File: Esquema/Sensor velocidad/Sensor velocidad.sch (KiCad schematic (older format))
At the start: 49 parts, among them J1 DB9_Female_MountingHoles, J2 DB9_Male_MountingHoles, J3 DB9_Female_MountingHoles, J4 DB9_Male_MountingHoles, J5 Conn_01x02_Male, U1 TCRT5000_GD, U2 TCRT5000_GD

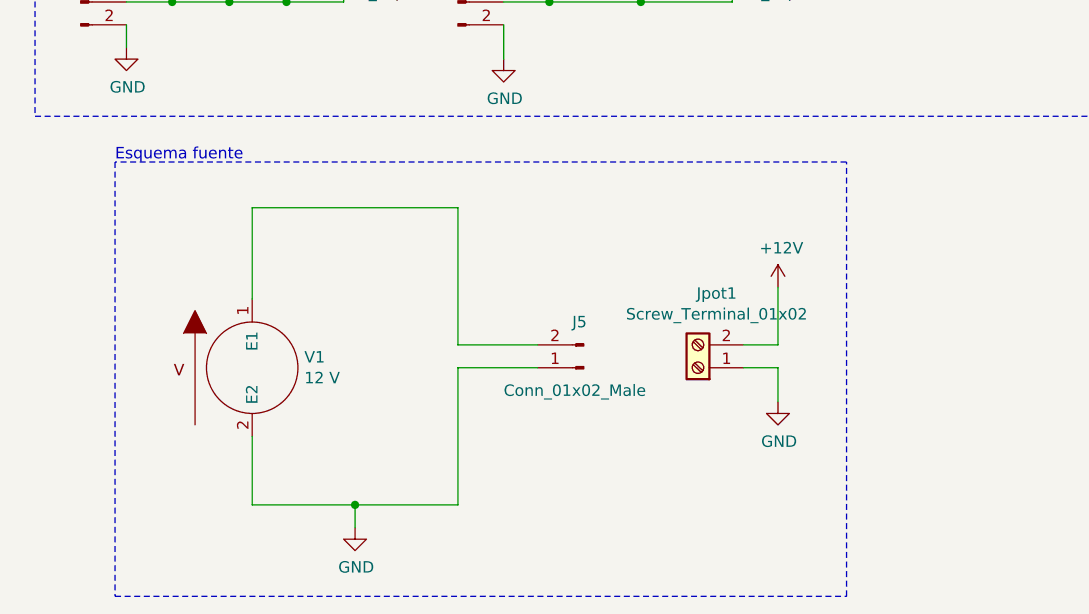
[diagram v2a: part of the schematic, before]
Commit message: Agregué labels de power port a la alimentación +12V y GND como recomendó la función ERC
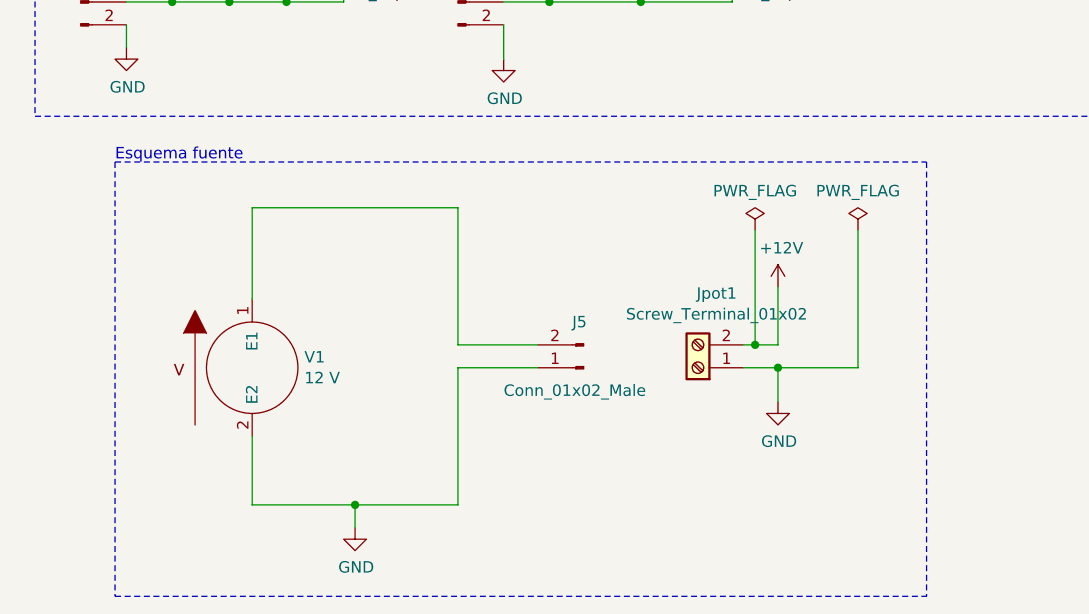
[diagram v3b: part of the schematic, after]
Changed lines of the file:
@@
 $EndComp
 Wire Wire Line
-	3700 6500 3850 6500
+	3700 6500 3750 6500
 Wire Wire Line
 	3850 6500 3850 6250
@@
 Wire Notes Line
 	950  5700 950  7600
-Wire Notes Line
-	950  7600 4150 7600
-Wire Notes Line
-	4150 7600 4150 5700
-Wire Notes Line
-	4150 5700 950  5700
 Text Notes 600  600  0    50   ~ 0
 Acondicionamiento sensor derecho
@@
 Text Notes 950  5700 0    50   ~ 0
 Esquema fuente
+$Comp
+L power:PWR_FLAG #FLG0101
+U 1 1 5EFE7C32
+P 3750 6000
+F 0 "#FLG0101" H 3750 6075 50  0001 C CNN
+F 1 "PWR_FLAG" H 3750 6173 50  0000 C CNN
+F 2 "" H 3750 6000 50  0001 C CNN
+F 3 "~" H 3750 6000 50  0001 C CNN
+	1    3750 6000
+	1    0    0    -1
+$EndComp
+Wire Wire Line
+	3750 6000 3750 6500
+Connection ~ 3750 6500
+Wire Wire Line
+	3750 6500 3850 6500
+$Comp
+L power:PWR_FLAG #FLG?
+U 1 1 5EFFC016
+P 4200 6000
+F 0 "#FLG?" H 4200 6075 50  0001 C CNN
+F 1 "PWR_FLAG" H 4200 6173 50  0000 C CNN
+F 2 "" H 4200 6000 50  0001 C CNN
+F 3 "~" H 4200 6000 50  0001 C CNN
+	1    4200 6000
+	1    0    0    -1
+$EndComp
+Wire Notes Line
+	4500 5700 4500 7600
+Wire Notes Line
+	950  7600 4500 7600
+Wire Notes Line
+	950  5700 4500 5700
+Wire Wire Line
+	4200 6000 4200 6600
+Wire Wire Line
+	4200 6600 3850 6600
+Connection ~ 3850 6600
 $EndSCHEMATC

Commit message: Empecé a agregar footprints a los componentes
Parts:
- J1, J3: footprint (none) -> Connector_Dsub:DSUB-9_Female_Horizontal_P2.77x2.84mm_EdgePinOffset4.94mm_Housed_MountingHolesOffset7.48mm
- J2, J4: footprint (none) -> Connector_Dsub:DSUB-9_Male_Horizontal_P2.77x2.84mm_EdgePinOffset4.94mm_Housed_MountingHolesOffset7.48mm
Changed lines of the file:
@@
-$EndComp
-$Comp
-L Connector:DB9_Female_MountingHoles J1
-U 1 1 5EC05B93
-P 5500 1650
-F 0 "J1" H 5680 1652 50  0000 L CNN
-F 1 "DB9_Female_MountingHoles" H 5000 900 50  0000 L CNN
-F 2 "" H 5500 1650 50  0001 C CNN
-F 3 " ~" H 5500 1650 50  0001 C CNN
-	1    5500 1650
-	1    0    0    -1
 $EndComp
 $Comp
@@
 F 0 "J2" H 7030 1559 50  0000 L CNN
 F 1 "DB9_Male_MountingHoles" H 6150 2250 50  0000 L CNN
-F 2 "" H 6850 1650 50  0001 C CNN
+F 2 "Connector_Dsub:DSUB-9_Male_Horizontal_P2.77x2.84mm_EdgePinOffset4.94mm_Housed_MountingHolesOffset7.48mm" H 6850 1650 50  0001 C CNN
 F 3 " ~" H 6850 1650 50  0001 C CNN
 	1    6850 1650
-	-1   0    0    1
-$EndComp
-$Comp
-L Connector:Screw_Terminal_01x02 Jpot1
-U 1 1 5EC730C8
-P 3500 6600
-F 0 "Jpot1" H 3418 6275 50  0000 C CNN
-F 1 "Screw_Terminal_01x02" H 3418 6366 50  0000 C CNN
-F 2 "" H 3500 6600 50  0001 C CNN
-F 3 "~" H 3500 6600 50  0001 C CNN
-	1    3500 6600
 	-1   0    0    1
 $EndComp
@@
 	1    0    0    -1
 $EndComp
-Wire Wire Line
-	3700 6500 3750 6500
 Wire Wire Line
 	3850 6500 3850 6250
@@
 F 0 "J3" H 5480 3952 50  0000 L CNN
 F 1 "DB9_Female_MountingHoles" H 4800 3200 50  0000 L CNN
-F 2 "" H 5300 3950 50  0001 C CNN
+F 2 "Connector_Dsub:DSUB-9_Female_Horizontal_P2.77x2.84mm_EdgePinOffset4.94mm_Housed_MountingHolesOffset7.48mm" H 5300 3950 50  0001 C CNN
 F 3 " ~" H 5300 3950 50  0001 C CNN
 	1    5300 3950
@@
 F 0 "J4" H 7030 3909 50  0000 L CNN
 F 1 "DB9_Male_MountingHoles" H 6150 4600 50  0000 L CNN
-F 2 "" H 6850 4000 50  0001 C CNN
+F 2 "Connector_Dsub:DSUB-9_Male_Horizontal_P2.77x2.84mm_EdgePinOffset4.94mm_Housed_MountingHolesOffset7.48mm" H 6850 4000 50  0001 C CNN
 F 3 " ~" H 6850 4000 50  0001 C CNN
 	1    6850 4000
@@
 Text Notes 600  600  0    50   ~ 0
 Acondicionamiento sensor derecho
+Text Notes 600  3150 0    50   ~ 0
+Acondicionamiento sensor izquierdo
 Text Notes 6350 600  0    50   ~ 0
 Esquema sensor derecho
-Text Notes 600  3150 0    50   ~ 0
-Acondicionamiento sensor izquierdo
 Text Notes 6350 3150 0    50   ~ 0
 Esquema sensor izquierdo
 Text Notes 950  5700 0    50   ~ 0
 Esquema fuente
+$Comp
+L Connector:Screw_Terminal_01x02 Jpot1
+U 1 1 5EC730C8
+P 3500 6600
+F 0 "Jpot1" H 3418 6275 50  0000 C CNN
+F 1 "Screw_Terminal_01x02" H 3418 6366 50  0000 C CNN
+F 2 "" H 3500 6600 50  0001 C CNN
+F 3 "~" H 3500 6600 50  0001 C CNN
+	1    3500 6600
+	-1   0    0    1
+$EndComp
 $Comp
 L power:PWR_FLAG #FLG0101
@@
 Wire Wire Line
 	3750 6000 3750 6500
+Wire Wire Line
+	3700 6500 3750 6500
+Wire Wire Line
+	3750 6500 3850 6500
 Connection ~ 3750 6500
-Wire Wire Line
-	3750 6500 3850 6500
-$Comp
-L power:PWR_FLAG #FLG?
+Wire Notes Line
+	4500 5700 4500 7600
+Wire Notes Line
+	950  7600 4500 7600
+Wire Notes Line
+	950  5700 4500 5700
+$Comp
+L power:PWR_FLAG #FLG0102
 U 1 1 5EFFC016
 P 4200 6000
-F 0 "#FLG?" H 4200 6075 50  0001 C CNN
+F 0 "#FLG0102" H 4200 6075 50  0001 C CNN
 F 1 "PWR_FLAG" H 4200 6173 50  0000 C CNN
 F 2 "" H 4200 6000 50  0001 C CNN
@@
 	1    0    0    -1
 $EndComp
-Wire Notes Line
-	4500 5700 4500 7600
-Wire Notes Line
-	950  7600 4500 7600
-Wire Notes Line
-	950  5700 4500 5700
 Wire Wire Line
 	4200 6000 4200 6600
@@
 	4200 6600 3850 6600
 Connection ~ 3850 6600
+$Comp
+L Connector:DB9_Female_MountingHoles J1
+U 1 1 5EC05B93
+P 5500 1650
+F 0 "J1" H 5680 1652 50  0000 L CNN
+F 1 "DB9_Female_MountingHoles" H 5000 900 50  0000 L CNN
+F 2 "Connector_Dsub:DSUB-9_Female_Horizontal_P2.77x2.84mm_EdgePinOffset4.94mm_Housed_MountingHolesOffset7.48mm" H 5500 1650 50  0001 C CNN
+F 3 " ~" H 5500 1650 50  0001 C CNN
+	1    5500 1650
+	1    0    0    -1
+$EndComp
 $EndSCHEMATC

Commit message: Agregué footprints a casi todos los componentes, me queda el TCRT5000 el cual hay un footprint en un repo de github
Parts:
- Jde1, Jde2, Jde3, Jde4, Jdr1, Jdr2, Jdr3, Jid1, Jie1, Jie2, Jie3, Jie4, Jii1, Jir1, Jir2, Jir3, Jvd1, Jved1, Jvi1, Jvri1: footprint (none) -> Connector_PinHeader_1.27mm:PinHeader_1x02_P1.27mm_Vertical
- Jpot1: footprint (none) -> TerminalBlock:TerminalBlock_bornier-2_P5.08mm
- R1, R10, R11, R12, R13, R14, R2, R3, R4, R5, R6, R7, R8, R9: footprint (none) -> Resistor_THT:R_Axial_DIN0207_L6.3mm_D2.5mm_P7.62mm_Horizontal
- RV1, RV2, RV3, RV4, RV5, RV6: footprint (none) -> Potentiometer_THT:Potentiometer_Bourns_3299W_Vertical

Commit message: Reasigné el footprint modificado a los jumpers
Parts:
- Jde1, Jde2, Jde3, Jde4, Jdr1, Jdr2, Jdr3, Jid1, Jie1, Jie2, Jie3, Jie4, Jii1, Jir1, Jir2, Jir3, Jvd1, Jved1, Jvi1, Jvri1: footprint Connector_PinHeader_1.27mm:PinHeader_1x02_P1.27mm_Vertical -> Proy_sen_vel:PinHeader_1x02_P1.27mm_Vertical
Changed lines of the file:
@@
 F 0 "Jde1" V 1350 1748 50  0000 L CNN
 F 1 "Jumper_NO_Small" V 1395 1748 50  0001 L CNN
-F 2 "Connector_PinHeader_1.27mm:PinHeader_1x02_P1.27mm_Vertical" H 1350 1700 50  0001 C CNN
+F 2 "Proy_sen_vel:PinHeader_1x02_P1.27mm_Vertical" H 1350 1700 50  0001 C CNN
 F 3 "~" H 1350 1700 50  0001 C CNN
 F 4 "Configuración de R 330 Ohm" V 1350 1700 50  0001 C CNN "Función"
@@
 F 0 "Jde2" V 1600 1748 50  0000 L CNN
 F 1 "Jumper_NO_Small" V 1645 1748 50  0001 L CNN
-F 2 "Connector_PinHeader_1.27mm:PinHeader_1x02_P1.27mm_Vertical" H 1600 1700 50  0001 C CNN
+F 2 "Proy_sen_vel:PinHeader_1x02_P1.27mm_Vertical" H 1600 1700 50  0001 C CNN
 F 3 "~" H 1600 1700 50  0001 C CNN
 F 4 "Configuración de R 470 Ohm" V 1600 1700 50  0001 C CNN "Función"
@@
 F 0 "Jde3" V 1850 1748 50  0000 L CNN
 F 1 "Jumper_NO_Small" V 1895 1748 50  0001 L CNN
-F 2 "Connector_PinHeader_1.27mm:PinHeader_1x02_P1.27mm_Vertical" H 1850 1700 50  0001 C CNN
+F 2 "Proy_sen_vel:PinHeader_1x02_P1.27mm_Vertical" H 1850 1700 50  0001 C CNN
 F 3 "~" H 1850 1700 50  0001 C CNN
 F 4 "Configuración de R 1 KOhm" V 1850 1700 50  0001 C CNN "Función"
@@
 F 0 "Jde4" V 2100 1748 50  0000 L CNN
 F 1 "Jumper_NO_Small" V 2145 1748 50  0001 L CNN
-F 2 "Connector_PinHeader_1.27mm:PinHeader_1x02_P1.27mm_Vertical" H 2100 1700 50  0001 C CNN
+F 2 "Proy_sen_vel:PinHeader_1x02_P1.27mm_Vertical" H 2100 1700 50  0001 C CNN
 F 3 "~" H 2100 1700 50  0001 C CNN
 F 4 "Configuración de R 330 Ohm" V 2100 1700 50  0001 C CNN "Función"
@@
 F 0 "Jdr1" V 3000 1298 50  0000 L CNN
 F 1 "Jumper_NO_Small" V 3045 1298 50  0001 L CNN
-F 2 "Connector_PinHeader_1.27mm:PinHeader_1x02_P1.27mm_Vertical" H 3000 1250 50  0001 C CNN
+F 2 "Proy_sen_vel:PinHeader_1x02_P1.27mm_Vertical" H 3000 1250 50  0001 C CNN
 F 3 "~" H 3000 1250 50  0001 C CNN
 F 4 "Configuración de red resistiva 1" V 3000 1250 50  0001 C CNN "Función"
@@
 F 0 "Jdr2" V 3400 1298 50  0000 L CNN
 F 1 "Jumper_NO_Small" V 3445 1298 50  0001 L CNN
-F 2 "Connector_PinHeader_1.27mm:PinHeader_1x02_P1.27mm_Vertical" H 3400 1250 50  0001 C CNN
+F 2 "Proy_sen_vel:PinHeader_1x02_P1.27mm_Vertical" H 3400 1250 50  0001 C CNN
 F 3 "~" H 3400 1250 50  0001 C CNN
 F 4 "Configuración de red resistiva 2" V 3400 1250 50  0001 C CNN "Función"
@@
 F 0 "Jdr3" V 3800 1298 50  0000 L CNN
 F 1 "Jumper_NO_Small" V 3845 1298 50  0001 L CNN
-F 2 "Connector_PinHeader_1.27mm:PinHeader_1x02_P1.27mm_Vertical" H 3800 1250 50  0001 C CNN
+F 2 "Proy_sen_vel:PinHeader_1x02_P1.27mm_Vertical" H 3800 1250 50  0001 C CNN
 F 3 "~" H 3800 1250 50  0001 C CNN
 F 4 "Configuración de red resistiva 3" V 3800 1250 50  0001 C CNN "Función"
@@
 F 0 "Jid1" V 1750 1298 50  0000 L CNN
 F 1 "Jumper_NO_Small" V 1795 1298 50  0001 L CNN
-F 2 "Connector_PinHeader_1.27mm:PinHeader_1x02_P1.27mm_Vertical" H 1750 1250 50  0001 C CNN
+F 2 "Proy_sen_vel:PinHeader_1x02_P1.27mm_Vertical" H 1750 1250 50  0001 C CNN
 F 3 "~" H 1750 1250 50  0001 C CNN
 F 4 "Medición corriente emisor derecho" V 1750 1250 50  0001 C CNN "Función"
@@
 F 0 "Jvd1" H 1008 2581 50  0000 C CNN
 F 1 "Conn_01x02_Male" H 1008 2490 50  0000 C CNN
-F 2 "Connector_PinHeader_1.27mm:PinHeader_1x02_P1.27mm_Vertical" H 900 2400 50  0001 C CNN
+F 2 "Proy_sen_vel:PinHeader_1x02_P1.27mm_Vertical" H 900 2400 50  0001 C CNN
 F 3 "~" H 900 2400 50  0001 C CNN
 F 4 "Medición tensión en emisor" H 900 2400 50  0001 C CNN "Función"
@@
 F 0 "Jved1" H 2708 2581 50  0000 C CNN
 F 1 "Conn_01x02_Male" H 2708 2490 50  0000 C CNN
-F 2 "Connector_PinHeader_1.27mm:PinHeader_1x02_P1.27mm_Vertical" H 2600 2400 50  0001 C CNN
+F 2 "Proy_sen_vel:PinHeader_1x02_P1.27mm_Vertical" H 2600 2400 50  0001 C CNN
 F 3 "~" H 2600 2400 50  0001 C CNN
 F 4 "Medición de osciloscopio receptor derecho" H 2600 2400 50  0001 C CNN "Función"
@@
 F 0 "Jie1" V 1200 4348 50  0000 L CNN
 F 1 "Jumper_NO_Small" V 1245 4348 50  0001 L CNN
-F 2 "Connector_PinHeader_1.27mm:PinHeader_1x02_P1.27mm_Vertical" H 1200 4300 50  0001 C CNN
+F 2 "Proy_sen_vel:PinHeader_1x02_P1.27mm_Vertical" H 1200 4300 50  0001 C CNN
 F 3 "~" H 1200 4300 50  0001 C CNN
 F 4 "Configuración de R 330 Ohm" V 1200 4300 50  0001 C CNN "Función"
@@
 F 0 "Jie2" V 1450 4348 50  0000 L CNN
 F 1 "Jumper_NO_Small" V 1495 4348 50  0001 L CNN
-F 2 "Connector_PinHeader_1.27mm:PinHeader_1x02_P1.27mm_Vertical" H 1450 4300 50  0001 C CNN
+F 2 "Proy_sen_vel:PinHeader_1x02_P1.27mm_Vertical" H 1450 4300 50  0001 C CNN
 F 3 "~" H 1450 4300 50  0001 C CNN
 F 4 "Configuración de R 470 Ohm" V 1450 4300 50  0001 C CNN "Función"
@@
 F 0 "Jie3" V 1700 4348 50  0000 L CNN
 F 1 "Jumper_NO_Small" V 1745 4348 50  0001 L CNN
-F 2 "Connector_PinHeader_1.27mm:PinHeader_1x02_P1.27mm_Vertical" H 1700 4300 50  0001 C CNN
+F 2 "Proy_sen_vel:PinHeader_1x02_P1.27mm_Vertical" H 1700 4300 50  0001 C CNN
 F 3 "~" H 1700 4300 50  0001 C CNN
 F 4 "Configuración de R 1 KOhm" V 1700 4300 50  0001 C CNN "Función"
@@
 F 0 "Jie4" V 1950 4348 50  0000 L CNN
 F 1 "Jumper_NO_Small" V 1995 4348 50  0001 L CNN
-F 2 "Connector_PinHeader_1.27mm:PinHeader_1x02_P1.27mm_Vertical" H 1950 4300 50  0001 C CNN
+F 2 "Proy_sen_vel:PinHeader_1x02_P1.27mm_Vertical" H 1950 4300 50  0001 C CNN
 F 3 "~" H 1950 4300 50  0001 C CNN
 F 4 "Configuración de R 330 Ohm" V 1950 4300 50  0001 C CNN "Función"
@@
 F 0 "Jir1" V 2850 3898 50  0000 L CNN
 F 1 "Jumper_NO_Small" V 2895 3898 50  0001 L CNN
-F 2 "Connector_PinHeader_1.27mm:PinHeader_1x02_P1.27mm_Vertical" H 2850 3850 50  0001 C CNN
+F 2 "Proy_sen_vel:PinHeader_1x02_P1.27mm_Vertical" H 2850 3850 50  0001 C CNN
 F 3 "~" H 2850 3850 50  0001 C CNN
 F 4 "Configuración de red resistiva 1" V 2850 3850 50  0001 C CNN "Función"
@@
 F 0 "Jir2" V 3250 3898 50  0000 L CNN
 F 1 "Jumper_NO_Small" V 3295 3898 50  0001 L CNN
-F 2 "Connector_PinHeader_1.27mm:PinHeader_1x02_P1.27mm_Vertical" H 3250 3850 50  0001 C CNN
+F 2 "Proy_sen_vel:PinHeader_1x02_P1.27mm_Vertical" H 3250 3850 50  0001 C CNN
 F 3 "~" H 3250 3850 50  0001 C CNN
 F 4 "Configuración de red resistiva 2" V 3250 3850 50  0001 C CNN "Función"
@@
 F 0 "Jir3" V 3650 3898 50  0000 L CNN
 F 1 "Jumper_NO_Small" V 3695 3898 50  0001 L CNN
-F 2 "Connector_PinHeader_1.27mm:PinHeader_1x02_P1.27mm_Vertical" H 3650 3850 50  0001 C CNN
+F 2 "Proy_sen_vel:PinHeader_1x02_P1.27mm_Vertical" H 3650 3850 50  0001 C CNN
 F 3 "~" H 3650 3850 50  0001 C CNN
 F 4 "Configuración de red resistiva 3" V 3650 3850 50  0001 C CNN "Función"
@@
 F 0 "Jii1" V 1600 3898 50  0000 L CNN
 F 1 "Jumper_NO_Small" V 1645 3898 50  0001 L CNN
-F 2 "Connector_PinHeader_1.27mm:PinHeader_1x02_P1.27mm_Vertical" H 1600 3850 50  0001 C CNN
+F 2 "Proy_sen_vel:PinHeader_1x02_P1.27mm_Vertical" H 1600 3850 50  0001 C CNN
 F 3 "~" H 1600 3850 50  0001 C CNN
 F 4 "Medición corriente emisor izquierdo" V 1600 3850 50  0001 C CNN "Función"
@@
 F 0 "Jvi1" H 908 5181 50  0000 C CNN
 F 1 "Conn_01x02_Male" H 908 5090 50  0000 C CNN
-F 2 "Connector_PinHeader_1.27mm:PinHeader_1x02_P1.27mm_Vertical" H 800 5000 50  0001 C CNN
+F 2 "Proy_sen_vel:PinHeader_1x02_P1.27mm_Vertical" H 800 5000 50  0001 C CNN
 F 3 "~" H 800 5000 50  0001 C CNN
 F 4 "Medición tensión en emisor" H 800 5000 50  0001 C CNN "Función"
@@
 F 0 "Jvri1" H 2558 5181 50  0000 C CNN
 F 1 "Conn_01x02_Male" H 2558 5090 50  0000 C CNN
-F 2 "Connector_PinHeader_1.27mm:PinHeader_1x02_P1.27mm_Vertical" H 2450 5000 50  0001 C CNN
+F 2 "Proy_sen_vel:PinHeader_1x02_P1.27mm_Vertical" H 2450 5000 50  0001 C CNN
 F 3 "~" H 2450 5000 50  0001 C CNN
 F 4 "Medición de osciloscopio receptor izquierdo" H 2450 5000 50  0001 C CNN "Función"

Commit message: Agrego el componente de sensado de distancia
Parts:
- U1, U2: footprint (none) -> Proy_sen_vel:TCRT5000
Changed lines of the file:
@@
 F 0 "U1" H 8000 2117 50  0000 C CNN
 F 1 "TCRT5000_GD" H 8000 2026 50  0000 C CNN
-F 2 "" H 8000 1600 50  0001 C CNN
+F 2 "Proy_sen_vel:TCRT5000" H 8000 1600 50  0001 C CNN
 F 3 "https://www.vishay.com/docs/83760/tcrt5000.pdf" H 8000 1900 50  0001 C CNN
 	1    8000 1800
@@
 F 0 "U2" H 8000 4467 50  0000 C CNN
 F 1 "TCRT5000_GD" H 8000 4376 50  0000 C CNN
-F 2 "" H 8000 3950 50  0001 C CNN
+F 2 "Proy_sen_vel:TCRT5000" H 8000 3950 50  0001 C CNN
 F 3 "https://www.vishay.com/docs/83760/tcrt5000.pdf" H 8000 4250 50  0001 C CNN
 	1    8000 4150

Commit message: Modificación de footprints en conectores db para que se vea reflejado en pcb
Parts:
- J1, J3: footprint Connector_Dsub:DSUB-9_Female_Horizontal_P2.77x2.84mm_EdgePinOffset4.94mm_Housed_MountingHolesOffset7.48mm -> Proy_sen_vel:DSUB-9_Female_Horizontal_P2.77x2.84mm_EdgePinOffset4.94mm_Housed_MountingHolesOffset7.48mm
- J2, J4: footprint Connector_Dsub:DSUB-9_Male_Horizontal_P2.77x2.84mm_EdgePinOffset4.94mm_Housed_MountingHolesOffset7.48mm -> Proy_sen_vel:DSUB-9_Male_Horizontal_P2.77x2.84mm_EdgePinOffset4.94mm_Housed_MountingHolesOffset7.48mm
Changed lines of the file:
@@
 F 0 "J2" H 7030 1559 50  0000 L CNN
 F 1 "DB9_Male_MountingHoles" H 6150 2250 50  0000 L CNN
-F 2 "Connector_Dsub:DSUB-9_Male_Horizontal_P2.77x2.84mm_EdgePinOffset4.94mm_Housed_MountingHolesOffset7.48mm" H 6850 1650 50  0001 C CNN
+F 2 "Proy_sen_vel:DSUB-9_Male_Horizontal_P2.77x2.84mm_EdgePinOffset4.94mm_Housed_MountingHolesOffset7.48mm" H 6850 1650 50  0001 C CNN
 F 3 " ~" H 6850 1650 50  0001 C CNN
 	1    6850 1650
@@
 F 0 "J3" H 5480 3952 50  0000 L CNN
 F 1 "DB9_Female_MountingHoles" H 4800 3200 50  0000 L CNN
-F 2 "Connector_Dsub:DSUB-9_Female_Horizontal_P2.77x2.84mm_EdgePinOffset4.94mm_Housed_MountingHolesOffset7.48mm" H 5300 3950 50  0001 C CNN
+F 2 "Proy_sen_vel:DSUB-9_Female_Horizontal_P2.77x2.84mm_EdgePinOffset4.94mm_Housed_MountingHolesOffset7.48mm" H 5300 3950 50  0001 C CNN
 F 3 " ~" H 5300 3950 50  0001 C CNN
 	1    5300 3950
@@
 F 0 "J4" H 7030 3909 50  0000 L CNN
 F 1 "DB9_Male_MountingHoles" H 6150 4600 50  0000 L CNN
-F 2 "Connector_Dsub:DSUB-9_Male_Horizontal_P2.77x2.84mm_EdgePinOffset4.94mm_Housed_MountingHolesOffset7.48mm" H 6850 4000 50  0001 C CNN
+F 2 "Proy_sen_vel:DSUB-9_Male_Horizontal_P2.77x2.84mm_EdgePinOffset4.94mm_Housed_MountingHolesOffset7.48mm" H 6850 4000 50  0001 C CNN
 F 3 " ~" H 6850 4000 50  0001 C CNN
 	1    6850 4000
@@
 F 0 "J1" H 5680 1652 50  0000 L CNN
 F 1 "DB9_Female_MountingHoles" H 5000 900 50  0000 L CNN
-F 2 "Connector_Dsub:DSUB-9_Female_Horizontal_P2.77x2.84mm_EdgePinOffset4.94mm_Housed_MountingHolesOffset7.48mm" H 5500 1650 50  0001 C CNN
+F 2 "Proy_sen_vel:DSUB-9_Female_Horizontal_P2.77x2.84mm_EdgePinOffset4.94mm_Housed_MountingHolesOffset7.48mm" H 5500 1650 50  0001 C CNN
 F 3 " ~" H 5500 1650 50  0001 C CNN
 	1    5500 1650
